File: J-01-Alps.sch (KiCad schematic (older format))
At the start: 17 parts, among them SW1 SW_Push, U1 ATmega32U4-AU, U4 PRTR5V0U2X, Y1 16MHz

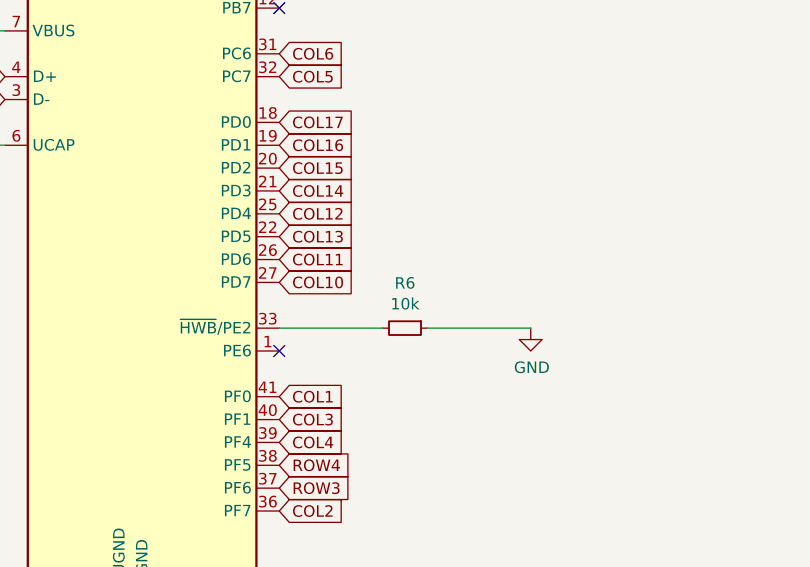
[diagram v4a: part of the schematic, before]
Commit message: Footprint changes
Changed all of the MX+Alps footprints to Alps only. Also added MX Stabilizer footprints.
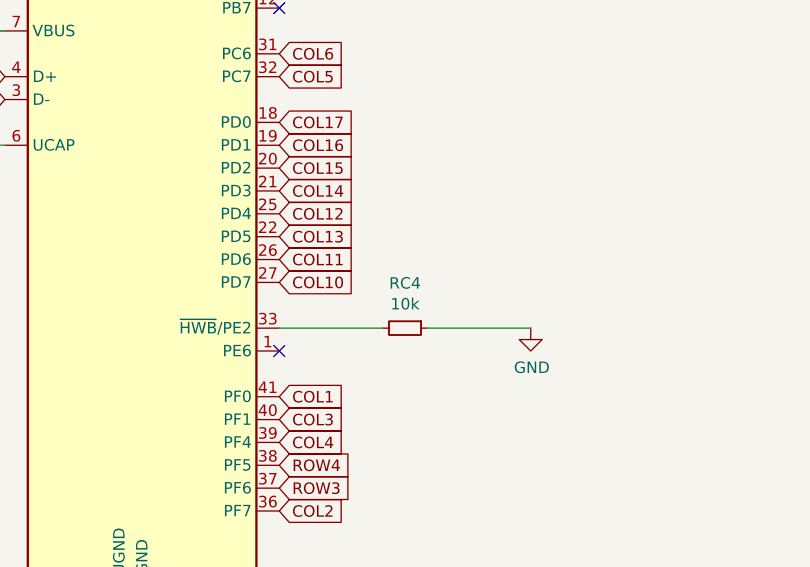
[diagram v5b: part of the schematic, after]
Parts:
- renumbered R6 to RC4
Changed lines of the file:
@@
 	5500 1350 5600 1350
 $Comp
-L Device:R_Small R6
+L Device:R_Small RC4
 U 1 1 61BC296D
 P 6650 3750
-F 0 "R6" V 6454 3750 50  0000 C CNN
+F 0 "RC4" V 6454 3750 50  0000 C CNN
 F 1 "10k" V 6545 3750 50  0000 C CNN
 F 2 "Resistor_SMD:R_0603_1608Metric_Pad0.98x0.95mm_HandSolder" H 6650 3750 50  0001 C CNN

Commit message: Continued work on layout
Layout refinements, USB traces, etc.
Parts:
- U4: footprint Package_TO_SOT_SMD:SOT-143 -> random-keyboard-parts:SOT143B
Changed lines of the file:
@@
 F 0 "U4" H 2644 2446 50  0000 L CNN
 F 1 "PRTR5V0U2X" H 2644 2355 50  0000 L CNN
-F 2 "Package_TO_SOT_SMD:SOT-143" H 2160 2400 50  0001 C CNN
+F 2 "random-keyboard-parts:SOT143B" H 2160 2400 50  0001 C CNN
 F 3 "https://assets.nexperia.com/documents/data-sheet/PRTR5V0U2X.pdf" H 2160 2400 50  0001 C CNN
 	1    2100 2400
@@
 F1 "matrix.sch" 50
 $EndSheet
-Text GLabel 6100 1950 2    50   Input ~ 0
-ROW0
-Text GLabel 6100 1850 2    50   Input ~ 0
-ROW1
 Text GLabel 6100 1650 2    50   Input ~ 0
 ROW2
@@
 Wire Wire Line
 	4200 3300 4200 3150
+Text GLabel 6100 1950 2    50   Input ~ 0
+ROW0
+Text GLabel 6100 1850 2    50   Input ~ 0
+ROW1
 $EndSCHEMATC

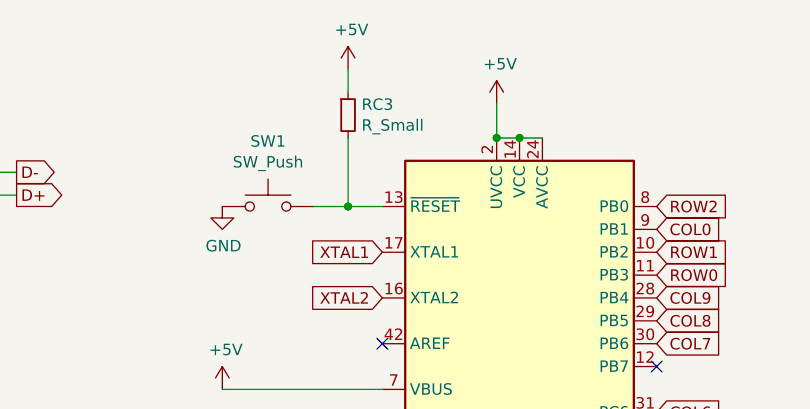
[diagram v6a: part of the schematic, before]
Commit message: Generate Gerber, BOM, and POS files
Generated production files, including Gerbers, BOM for JLCPCB, and positioning files (specific to JLCPCB).
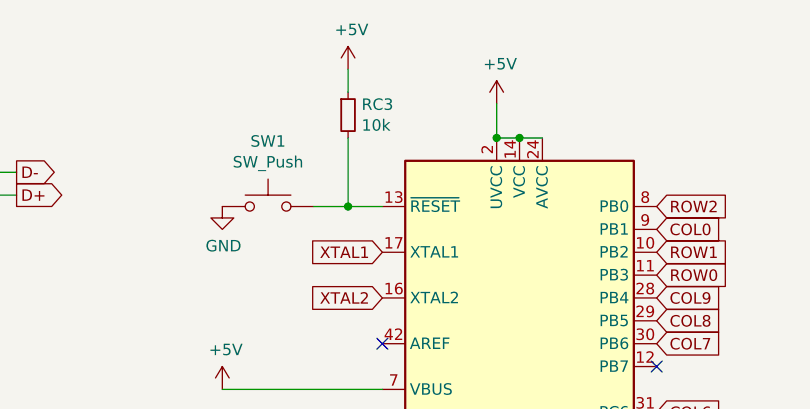
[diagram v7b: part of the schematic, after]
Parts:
- C2: LCSC (none) -> C15849
- C5: LCSC (none) -> C19702
- C6, C7, C8: LCSC (none) -> C14663
- CC1, CC2: LCSC (none) -> C1653
- F1: LCSC (none) -> C315893
- JST2: LCSC (none) -> C160404
- RC1, RC2: LCSC (none) -> C23345
- RC3: value R_Small -> 10k; LCSC (none) -> C25804
- RC4: LCSC (none) -> C25804
- U1: LCSC (none) -> C44854
- U4: LCSC (none) -> C12333
- Y1: LCSC (none) -> C255906
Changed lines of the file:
@@
 F 2 "Package_QFP:TQFP-44_10x10mm_P0.8mm" H 5500 3150 50  0001 C CIN
 F 3 "http://ww1.microchip.com/downloads/en/DeviceDoc/Atmel-7766-8-bit-AVR-ATmega16U4-32U4_Datasheet.pdf" H 5500 3150 50  0001 C CNN
+F 4 "C44854" H 5500 3150 50  0001 C CNN "LCSC"
 	1    5500 3150
 	1    0    0    -1
@@
 F 2 "Resistor_SMD:R_0603_1608Metric_Pad0.98x0.95mm_HandSolder" H 6650 3750 50  0001 C CNN
 F 3 "~" H 6650 3750 50  0001 C CNN
+F 4 "C25804" H 6650 3750 50  0001 C CNN "LCSC"
 	1    6650 3750
 	0    1    1    0
@@
 F 2 "Capacitor_SMD:C_0603_1608Metric_Pad1.08x0.95mm_HandSolder" H 4200 3050 50  0001 C CNN
 F 3 "~" H 4200 3050 50  0001 C CNN
+F 4 "C15849" H 4200 3050 50  0001 C CNN "LCSC"
 	1    4200 3050
 	1    0    0    -1
@@
 F 2 "Connector_JST:JST_SH_SM04B-SRSS-TB_1x04-1MP_P1.00mm_Horizontal" H 1250 1500 50  0001 C CNN
 F 3 "~" H 1250 1500 50  0001 C CNN
+F 4 " C160404" H 1250 1500 50  0001 C CNN "LCSC"
 	1    1250 1500
 	-1   0    0    -1
@@
 F 2 "random-keyboard-parts:SOT143B" H 2160 2400 50  0001 C CNN
 F 3 "https://assets.nexperia.com/documents/data-sheet/PRTR5V0U2X.pdf" H 2160 2400 50  0001 C CNN
+F 4 "C12333" H 2100 2400 50  0001 C CNN "LCSC"
 	1    2100 2400
 	1    0    0    -1
@@
 F 2 "Fuse:Fuse_1206_3216Metric_Pad1.42x1.75mm_HandSolder" H 1800 3500 50  0001 L CNN
 F 3 "~" H 1750 3700 50  0001 C CNN
+F 4 "C315893" H 1750 3700 50  0001 C CNN "LCSC"
 	1    1750 3700
 	0    1    1    0
@@
 F 2 "Resistor_SMD:R_0603_1608Metric_Pad0.98x0.95mm_HandSolder" H 3000 1500 50  0001 C CNN
 F 3 "~" H 3000 1500 50  0001 C CNN
+F 4 "C23345" H 3000 1500 50  0001 C CNN "LCSC"
 	1    3000 1500
 	0    1    1    0
@@
 F 2 "Resistor_SMD:R_0603_1608Metric_Pad0.98x0.95mm_HandSolder" H 3000 1600 50  0001 C CNN
 F 3 "~" H 3000 1600 50  0001 C CNN
+F 4 "C23345" H 3000 1600 50  0001 C CNN "LCSC"
 	1    3000 1600
 	0    -1   -1   0
@@
 P 4750 1250
 F 0 "RC3" H 4809 1296 50  0000 L CNN
-F 1 "R_Small" H 4809 1205 50  0000 L CNN
+F 1 "10k" H 4809 1205 50  0000 L CNN
 F 2 "Resistor_SMD:R_0603_1608Metric_Pad0.98x0.95mm_HandSolder" H 4750 1250 50  0001 C CNN
 F 3 "~" H 4750 1250 50  0001 C CNN
+F 4 "C25804" H 4750 1250 50  0001 C CNN "LCSC"
 	1    4750 1250
 	1    0    0    -1
@@
 F 2 "Crystal:Crystal_SMD_3225-4Pin_3.2x2.5mm_HandSoldering" H 1800 5800 50  0001 C CNN
 F 3 "~" H 1800 5800 50  0001 C CNN
+F 4 "C255906" H 1800 5800 50  0001 C CNN "LCSC"
 	1    1800 5800
 	0    1    1    0
@@
 F 2 "Capacitor_SMD:C_0603_1608Metric_Pad1.08x0.95mm_HandSolder" H 1400 5700 50  0001 C CNN
 F 3 "~" H 1400 5700 50  0001 C CNN
+F 4 "C1653" H 1400 5700 50  0001 C CNN "LCSC"
 	1    1400 5700
 	0    1    1    0
@@
 F 2 "Capacitor_SMD:C_0603_1608Metric_Pad1.08x0.95mm_HandSolder" H 1400 5900 50  0001 C CNN
 F 3 "~" H 1400 5900 50  0001 C CNN
+F 4 "C1653" H 1400 5900 50  0001 C CNN "LCSC"
 	1    1400 5900
 	0    1    1    0
@@
 F 2 "Capacitor_SMD:C_0603_1608Metric_Pad1.08x0.95mm_HandSolder" H 1300 4550 50  0001 C CNN
 F 3 "~" H 1300 4550 50  0001 C CNN
+F 4 "C19702" H 1300 4550 50  0001 C CNN "LCSC"
 	1    1300 4550
 	1    0    0    -1
@@
 F 2 "Capacitor_SMD:C_0603_1608Metric_Pad1.08x0.95mm_HandSolder" H 1700 4550 50  0001 C CNN
 F 3 "~" H 1700 4550 50  0001 C CNN
+F 4 "C14663" H 1700 4550 50  0001 C CNN "LCSC"
 	1    1700 4550
 	1    0    0    -1
@@
 F 2 "Capacitor_SMD:C_0603_1608Metric_Pad1.08x0.95mm_HandSolder" H 2100 4550 50  0001 C CNN
 F 3 "~" H 2100 4550 50  0001 C CNN
+F 4 "C14663" H 2100 4550 50  0001 C CNN "LCSC"
 	1    2100 4550
 	1    0    0    -1
@@
 F 2 "Capacitor_SMD:C_0603_1608Metric_Pad1.08x0.95mm_HandSolder" H 2500 4550 50  0001 C CNN
 F 3 "~" H 2500 4550 50  0001 C CNN
+F 4 "C14663" H 2500 4550 50  0001 C CNN "LCSC"
 	1    2500 4550
 	1    0    0    -1

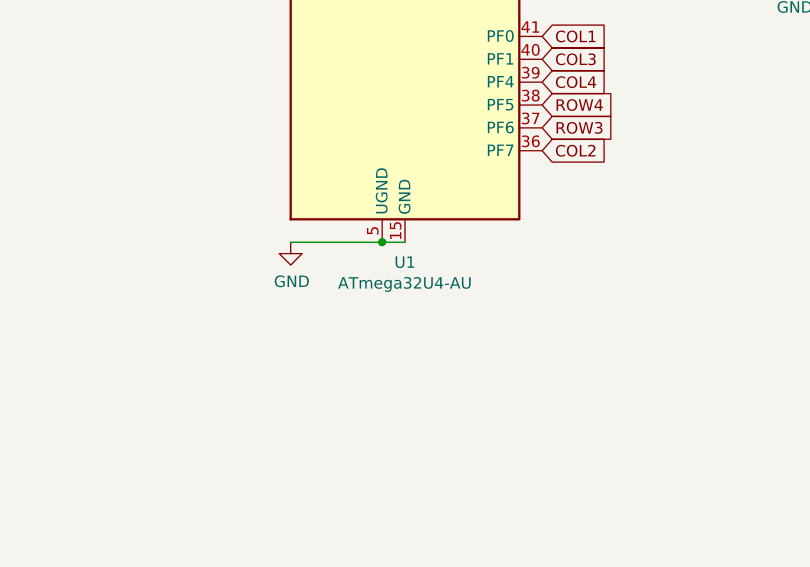
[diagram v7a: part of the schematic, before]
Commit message: Modifications for QFN footprint
Modifications for ATmega32U4-MU. Rerouting of USB traces, 5V lines, and other supporting components.
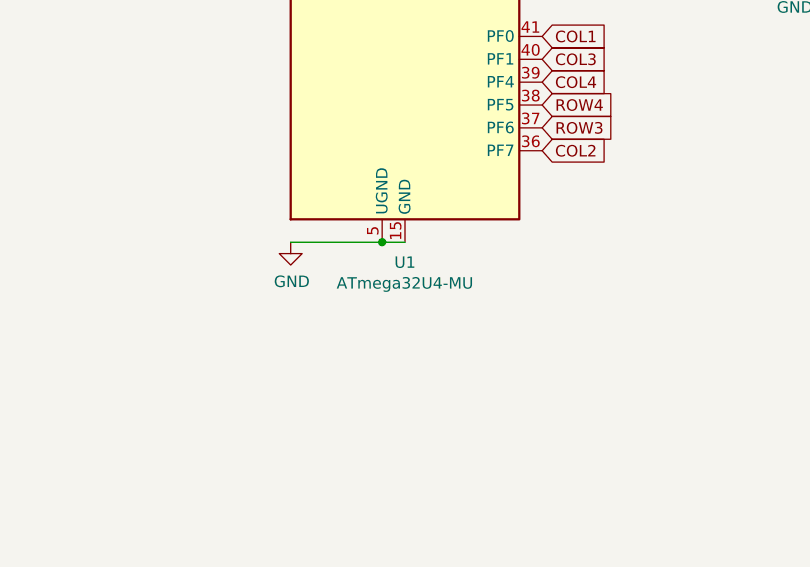
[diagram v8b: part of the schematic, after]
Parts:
- U1: value ATmega32U4-AU -> ATmega32U4-MU; footprint Package_QFP:TQFP-44_10x10mm_P0.8mm -> Package_DFN_QFN:QFN-44-1EP_7x7mm_P0.5mm_EP5.15x5.15mm; LCSC C44854 -> (none)
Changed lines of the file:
@@
 P 5500 3150
 F 0 "U1" H 5500 1261 50  0000 C CNN
-F 1 "ATmega32U4-AU" H 5500 1170 50  0000 C CNN
-F 2 "Package_QFP:TQFP-44_10x10mm_P0.8mm" H 5500 3150 50  0001 C CIN
+F 1 "ATmega32U4-MU" H 5500 1170 50  0000 C CNN
+F 2 "Package_DFN_QFN:QFN-44-1EP_7x7mm_P0.5mm_EP5.15x5.15mm" H 5500 3150 50  0001 C CIN
 F 3 "http://ww1.microchip.com/downloads/en/DeviceDoc/Atmel-7766-8-bit-AVR-ATmega16U4-32U4_Datasheet.pdf" H 5500 3150 50  0001 C CNN
-F 4 "C44854" H 5500 3150 50  0001 C CNN "LCSC"
+F 4 "" H 5500 3150 50  0001 C CNN "LCSC"
 	1    5500 3150
 	1    0    0    -1
